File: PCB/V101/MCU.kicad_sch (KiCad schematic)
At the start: 17 parts, among them U501 STM32G431CBUx, Y501 Crystal_GND24, Y502 Crystal_GND24

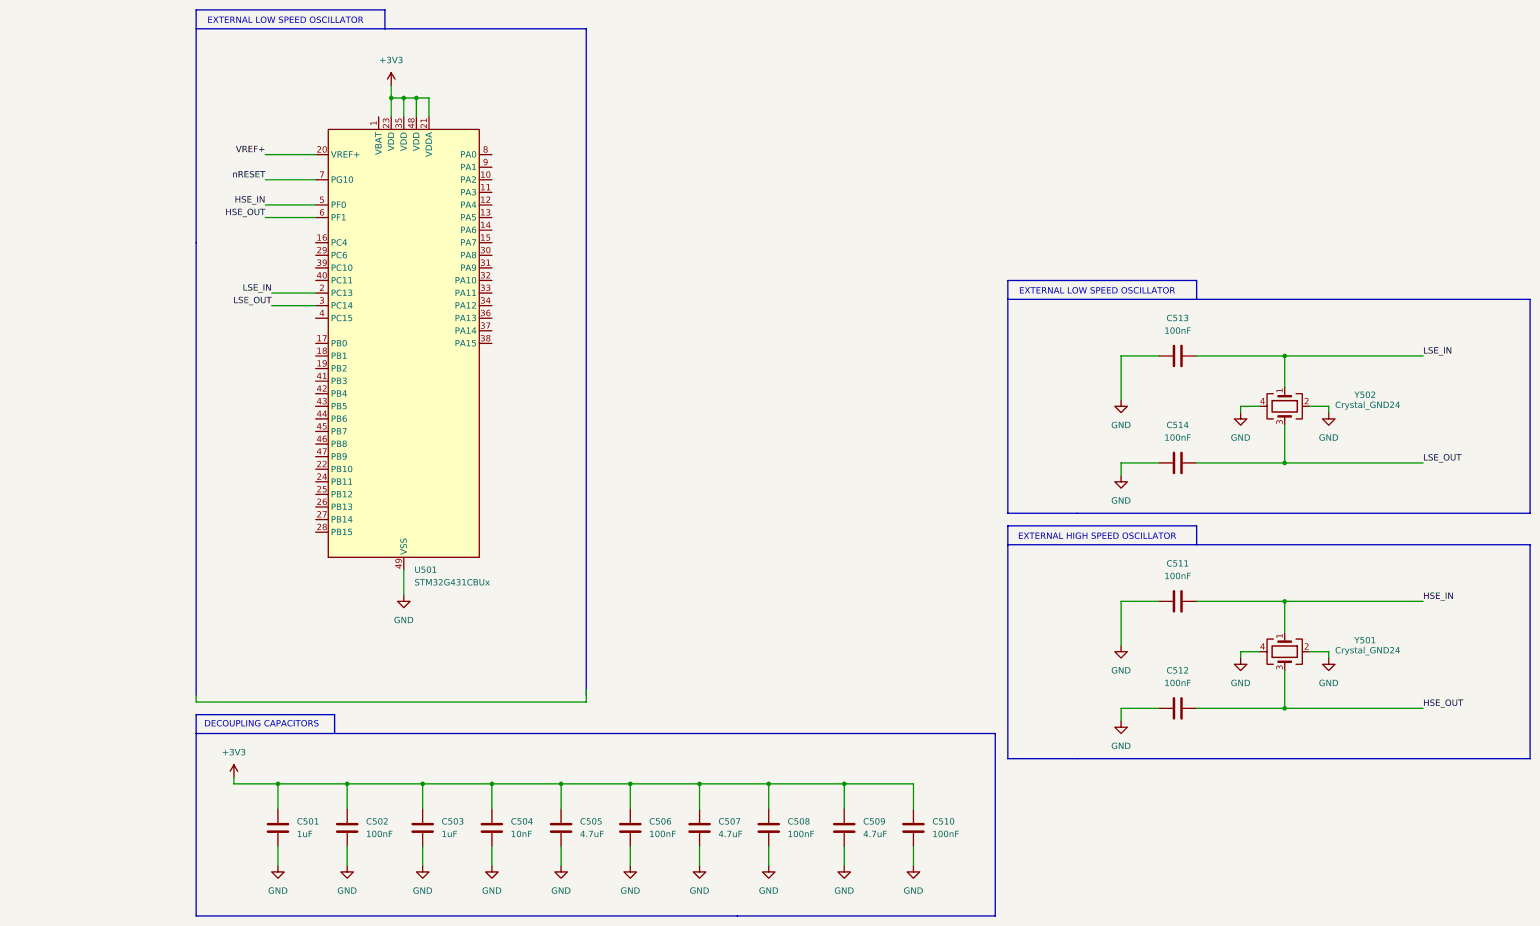
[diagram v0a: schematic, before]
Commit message: Updated PCB with PA & Block Diagram
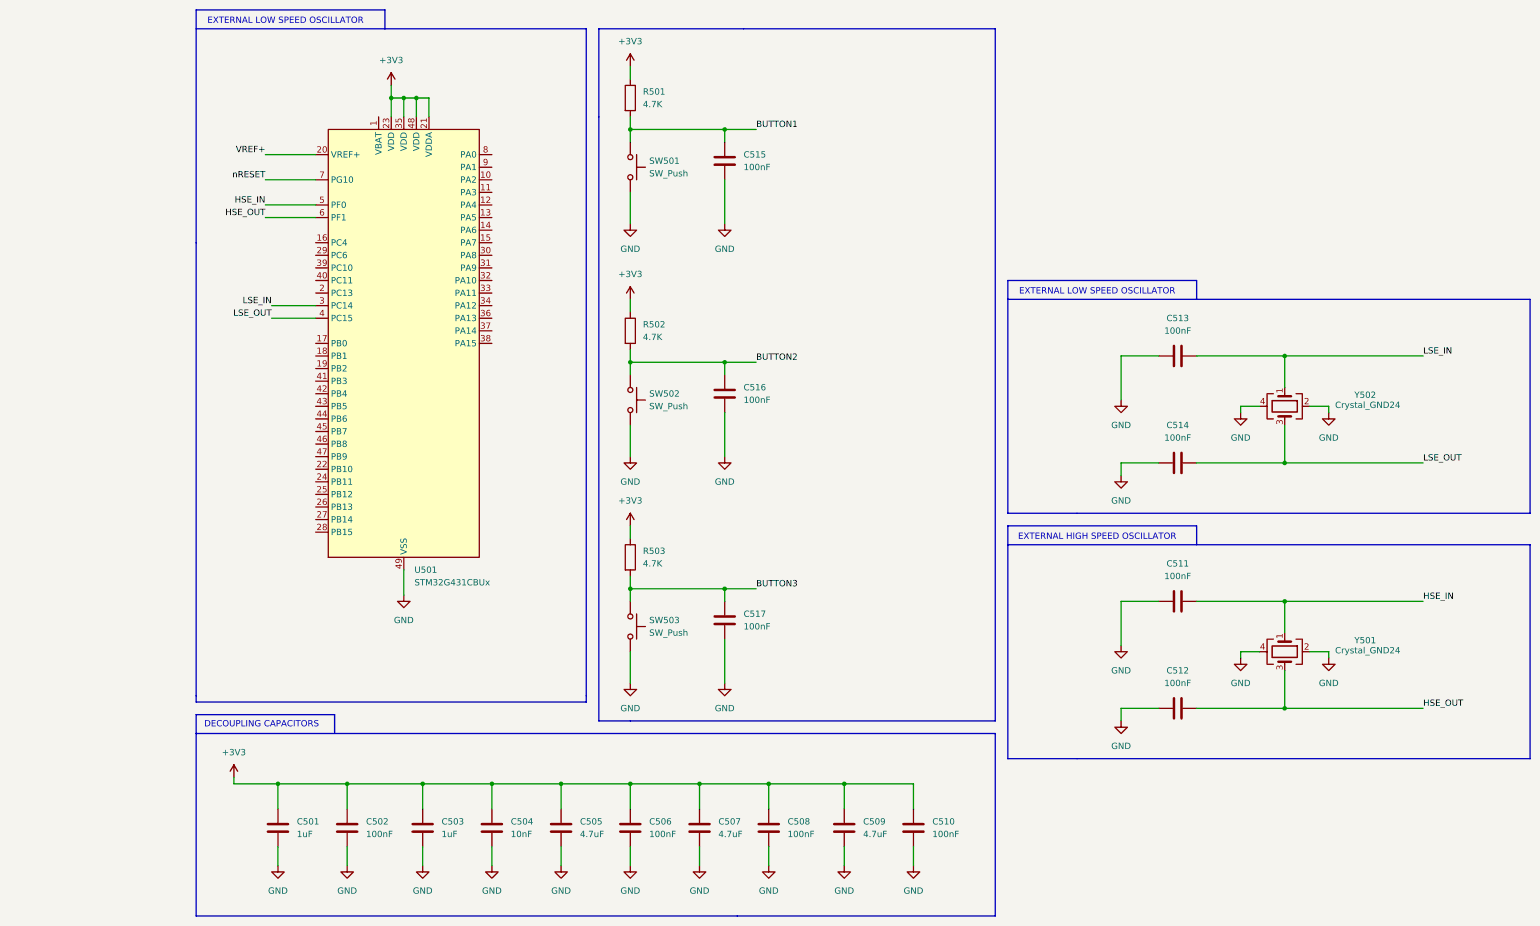
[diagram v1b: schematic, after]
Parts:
- added C515, C516, C517: 100nF, Capacitor_SMD:C_0402_1005Metric_Pad0.74x0.62mm_HandSolder, symbol Device:C
- added R501, R502, R503: 4.7K, symbol Device:R
- added SW501, SW502, SW503: SW_Push, symbol Switch:SW_Push
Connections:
- net +3V3: now also R501.1, R502.1, R503.1
- net GND: now also C515.2, C516.2, C517.2, SW501.2, SW502.2, SW503.2
- net LSE_IN: now also U501.3 (PC14); no longer U501.2 (PC13)
- net LSE_OUT: now also U501.4 (PC15); no longer U501.3 (PC14)
- new net BUTTON1: C515.1, R501.2, SW501.1
- new net BUTTON2: C516.1, R502.2, SW502.1
- new net BUTTON3: C517.1, R503.2, SW503.1

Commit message: Updated PCB
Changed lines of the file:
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@@
+		)
+	)
+	(global_label "I2C1_SCL"
+		(shape input)
+		(at -20.32 77.47 0)
+		(fields_autoplaced yes)
+		(effects
+			(font
+				(size 1.27 1.27)
+			)
+			(justify left)
+		)
+		(property "Intersheetrefs" "${INTERSHEET_REFS}"
+			(at -8.5658 77.47 0)
+			(effects
+				(font
+					(size 1.27 1.27)
+				)
+				(justify left)
+				(hide yes)
+			)
+		)
+	)
+	(global_label "I2C1_SDA"
+		(shape input)
+		(at -20.32 80.01 0)
+		(fields_autoplaced yes)
+		(effects
+			(font
+				(size 1.27 1.27)
+			)
+			(justify left)
+		)
+		(property "Intersheetrefs" "${INTERSHEET_REFS}"
+			(at -8.5053 80.01 0)
+			(effects
+				(font
+					(size 1.27 1.27)
+				)
+				(justify left)
+				(hide yes)
+			)
+		)
+	)
+	(global_label "I2C2_SDA"
+		(shape input)
+		(at -20.32 86.36 0)
+		(fields_autoplaced yes)
+		(effects
+			(font
+				(size 1.27 1.27)
+			)
+			(justify left)
+		)
+		(property "Intersheetrefs" "${INTERSHEET_REFS}"
+			(at -8.5053 86.36 0)
+			(effects
+				(font
+					(size 1.27 1.27)
+				)
+				(justify left)
+				(hide yes)
+			)
+		)
+	)
+	(global_label "USART1_DE_PIN"
+		(shape input)
+		(at -2.54 71.12 180)
+		(fields_autoplaced yes)
+		(effects
+			(font
+				(size 1.27 1.27)
+			)
+			(justify right)
+		)
+		(property "Intersheetrefs" "${INTERSHEET_REFS}"
+			(at -20.1604 71.12 0)
+			(effects
+				(font
+					(size 1.27 1.27)
+				)
+				(justify right)
+				(hide yes)
+			)
+		)
+	)
+	(global_label "USART1_RE_PIN"
+		(shape input)
+		(at -2.54 68.58 180)
+		(fields_autoplaced yes)
+		(effects
+			(font
+				(size 1.27 1.27)
+			)
+			(justify right)
+		)
+		(property "Intersheetrefs" "${INTERSHEET_REFS}"
+			(at -20.1604 68.58 0)
+			(effects
+				(font
+					(size 1.27 1.27)
+				)
+				(justify right)
+				(hide yes)
+			)
+		)
+	)
+	(global_label "I2C2_SCL"
+		(shape input)
+		(at -20.32 83.82 0)
+		(fields_autoplaced yes)
+		(effects
+			(font
+				(size 1.27 1.27)
+			)
+			(justify left)
+		)
+		(property "Intersheetrefs" "${INTERSHEET_REFS}"
+			(at -8.5658 83.82 0)
+			(effects
+				(font
+					(size 1.27 1.27)
+				)
+				(justify left)
+				(hide yes)
+			)
+		)
+	)
+	(global_label "USART1_TX_PIN"
+		(shape input)
+		(at -2.54 73.66 180)
+		(fields_autoplaced yes)
+		(effects
+			(font
+				(size 1.27 1.27)
+			)
+			(justify right)
+		)
+		(property "Intersheetrefs" "${INTERSHEET_REFS}"
+			(at -19.9185 73.66 0)
+			(effects
+				(font
+					(size 1.27 1.27)
+				)
+				(justify right)
+				(hide yes)
+			)
+		)
+	)
+	(global_label "USART1_RX_PIN"
+		(shape input)
+		(at -2.54 66.04 180)
+		(fields_autoplaced yes)
+		(effects
+			(font
+				(size 1.27 1.27)
+			)
+			(justify right)
+		)
+		(property "Intersheetrefs" "${INTERSHEET_REFS}"
+			(at -20.2209 66.04 0)
+			(effects
+				(font
+					(size 1.27 1.27)
+				)
+				(justify right)
+				(hide yes)
+			)
 		)
 	)

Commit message: Updated Layout
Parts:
- removed U501: STM32G431CBUx, Package_DFN_QFN:QFN-48-1EP_7x7mm_P0.5mm_EP5.6x5.6mm, symbol MCU_ST_STM32G4:STM32G431CBUx
- added U501: STM32G431CBTx, Package_QFP:LQFP-48_7x7mm_P0.5mm, symbol MCU_ST_STM32G4:STM32G431CBTx
- R501, R502, R503: footprint (none) -> Resistor_SMD:R_0603_1608Metric_Pad0.98x0.95mm_HandSolder
- renumbered C515 to C508, C516 to C509, C517 to C510, C508 to C511, C509 to C512, C510 to C513, C513 to C514, C514 to C515, C511 to C516, C512 to C517, Y502 to Y501, Y501 to Y502
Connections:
- net +3V3: now also U501.1 (VBAT), U501.21 (VDDA), U501.24 (VDD), U501.36 (VDD), U501.48 (VDD)
- net GND: now also U501.19 (VSSA), U501.23 (VSS), U501.35 (VSS), U501.47 (VSS)
- net HSE_IN: now also U501.5 (PF0)
- net HSE_OUT: now also U501.6 (PF1)
- net LSE_IN: now also U501.3 (PC14)
- net LSE_OUT: now also U501.4 (PC15)
- net VREF+: now also U501.20 (VREF+)
- net nRESET: now also U501.7 (PG10)
